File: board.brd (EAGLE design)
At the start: 25 x 23.8 mm, 31 parts, among them SW1 JST_SM02B-SRSS-TB, U2 FT232RQ, U3 ATTINY1607-MFR, U4 RV-8803, X2 JST_SM02B-SRSS-TB

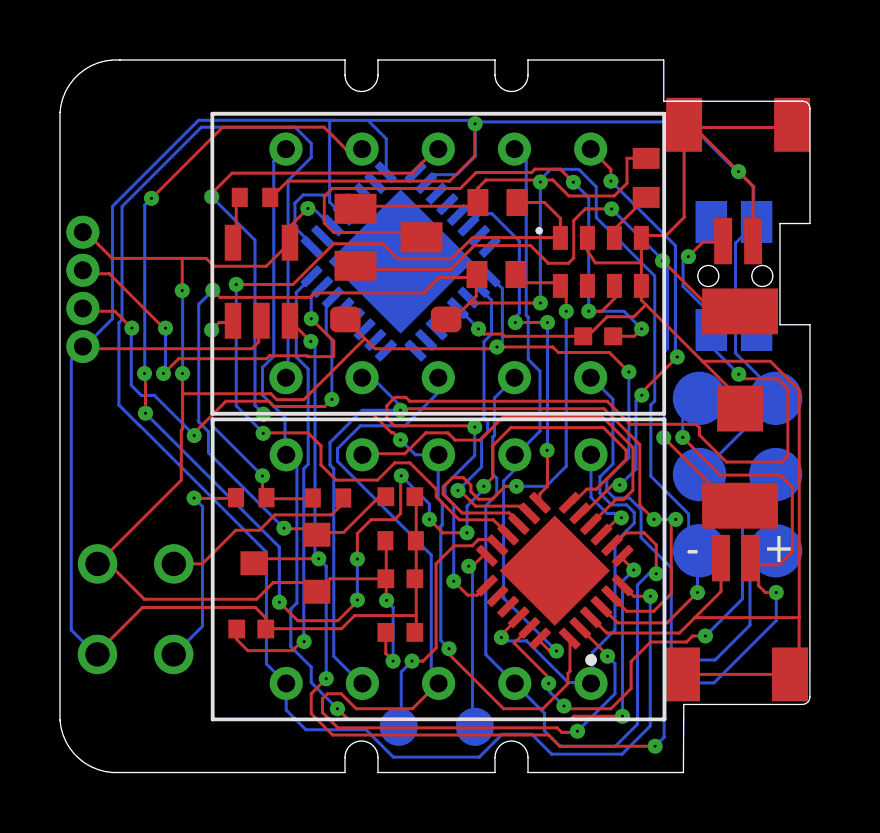
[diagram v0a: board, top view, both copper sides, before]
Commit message: 4 layer brd design for watch PCB added
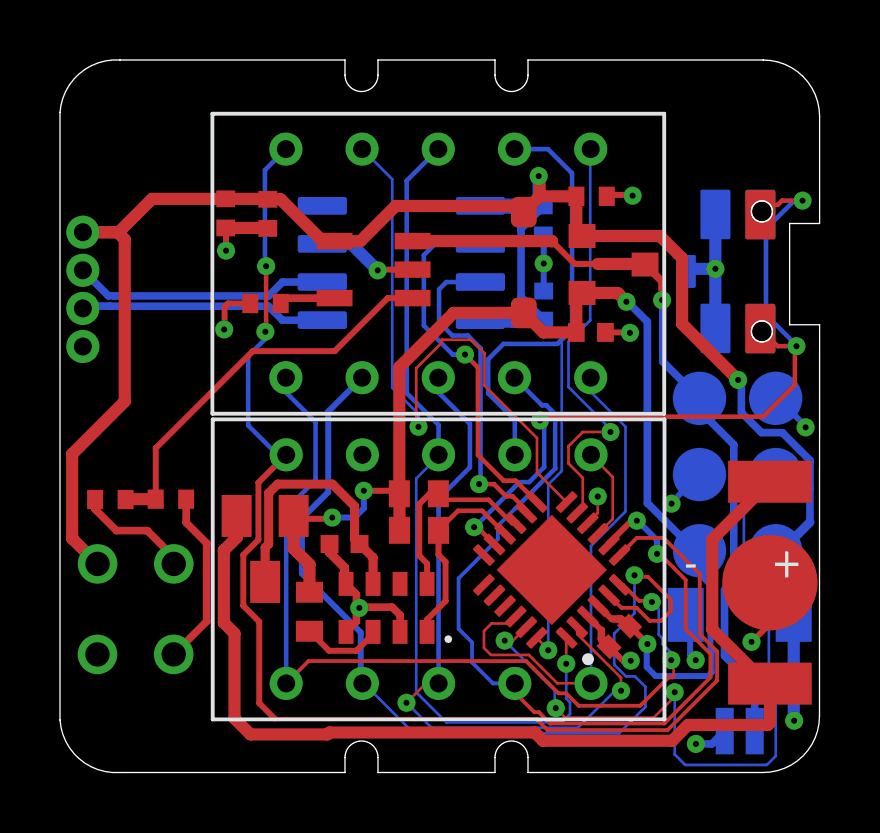
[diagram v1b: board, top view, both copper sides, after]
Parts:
- removed PC0, PC1: TESTPAD_TPSQB1,27, ARDUINO_3V_TTL_INTERFACE_2_PI:TESTPAD_B1,27
- removed SW1: JST_SM02B-SRSS-TB, MY_CLOCK_LIB_COMPONENTS:JST-SM02B-SRSS-TB
- removed U$9: EVQP7L01P, MY_CLOCK_LIB_COMPONENTS:EVQP7L01P
- removed U2: FT232RQ, FT232RQ:QFN50P500X500X90-33N
- added C3, C7: 100nF, MY_CAP_LIB:CAPC1005X60
- added U$4: PTS840ESDPMSMTRLF, MY_CLOCK_LIB_COMPONENTS:PTS840ESDPMSMTRLF
- added U$6: CH330N, MY_CLOCK_LIB_COMPONENTS:CH330N
- 1.55V-8MAH: value KEYSTONE-2294TR -> BK-414-TR; device MY_CLOCK_LIB_COMPONENTS:KEYSTONE-2994TR -> MY_CLOCK_LIB_COMPONENTS:BK-414-TR
- BOT, TOP: value 0.28"-2DIGIT-7SEGEMNT -> 0.28-2DIGIT-7SEGEMNT; device MY_CLOCK_LIB_COMPONENTS:2_DIGIT_0.28" -> MY_CLOCK_LIB_COMPONENTS:2_DIGIT_0.28
- moved R7 18.3 mm to (9.07, 6.11)
- moved C5 16.7 mm to (16.9, 19.2), flipped to the bottom, turned to 270 degrees
- moved C1 15.1 mm to (6.27, 19.4), turned to 270 degrees
- moved U$3 14.7 mm to (19.2, 17.7), turned to 270 degrees
- moved U4 13.6 mm to (11.6, 6.24), turned to 180 degrees
- moved R6 13.1 mm to (18.5, 20.0)
- moved C2 12.9 mm to (7.68, 19.4), turned to 270 degrees
- moved R4 11.2 mm to (12.7, 8.82)
- moved D2 11.2 mm to (7.59, 8.20), turned to 180 degrees
- moved C6 10.9 mm to (10.2, 8.37)
- moved C4 8.38 mm to (18.4, 15.4)
- moved R5 7.75 mm to (12.7, 10.0)
- moved R1 7.26 mm to (2.43, 9.85), turned to 0 degrees
- moved 1.55V-8MAH 5.89 mm to (24.4, 7.08)
- moved X2 5.77 mm to (23.4, 2.13), flipped to the bottom, turned to 0 degrees
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- renumbered BATTERY_CHARGED_GREEN to GREEN, BATT_CONNECTED_YELLOW to YELLOW
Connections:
- net N$2 renamed CHARGER_STAT
- net N$4 renamed LEDY_K
- net N$5 renamed CHARGER_PROG
- net N$6 renamed LEDG_A
- removed net EXP: U2.33
- removed net N$11: C5.1, U2.16
- removed net PC0: PC0.TP, U3.17
- removed net PC1: PC1.TP, U3.18
- removed net USBDM: U$5.P$2, U2.15
- removed net USBDP: U$5.P$3, U2.14
- new net USBD_N: U$5.USBD_N, U$6.D_N
- new net USBD_P: U$5.USBD_P, U$6.D_P
- net GND: now also 1.55V-8MAH.-, C3.2, C7.2, U$4.1, U$4.2, U$4.5, U$5.GND, U$6.GND; no longer 1.55V-8MAH.P$1, SW1.1, SW1.M1, SW1.M2, U$5.P$4, U$9.P$2, U2.17, U2.20, U2.24, U2.26, U2.4
- net RX: now also U$6.RXI; no longer U2.2
- net SW1: now also U$4.3, U$4.4, U$4.B3, U$4.B4, U3.17; no longer SW1.2, U$9.P$3, U3.19
- net TX: now also U$6.TXD; no longer U2.30
- net VBATT: now also 1.55V-8MAH.1+, 1.55V-8MAH.2+; no longer 1.55V-8MAH.P$2, 1.55V-8MAH.P$3
- net VCC: now also C7.1
- net V_USB: now also C3.1, C5.1, U$5.V_USB, U$6.V3, U$6.VCC; no longer U$5.P$1, U2.1, U2.19
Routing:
- net GND: track 151.7 -> 35.5 mm, vias 3 -> 15
- net COMM1: track 46.4 -> 21.0 mm, vias 10 -> 1
- net SEG_E: track 54.1 -> 29.4 mm, vias 1 -> 2
- net SCL: track 30.1 -> 6.55 mm, vias 2 -> 0
- net VCC: track 63.9 -> 41.4 mm, vias 5 -> 4
- net V_LIPO: track 46.7 -> 25.4 mm, vias 6 -> 1
- net N$11: track 15.5 -> 0.00 mm, vias 1 -> 0
- net USBDP: track 15.5 -> 0.00 mm, vias 3 -> 0
- net USBDM: track 13.8 -> 0.00 mm, vias 3 -> 0
- net V_USB: track 74.1 -> 60.6 mm, vias 7 -> 2
- net VDD1: track 22.2 -> 9.15 mm, vias 3 -> 0
- net SW1: track 35.5 -> 25.3 mm
- net SDA: track 16.1 -> 6.53 mm, vias 2 -> 0
- net VBATT: track 26.1 -> 35.2 mm, vias 3 -> 0
- net SEG_C: track 32.1 -> 23.1 mm
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- added copper zone on layer 15, net GND
- added copper zone on layer 2, net GND
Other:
- board size 25 x 23.8 mm -> 25.3 x 23.8 mm
- board text removed: "P7"
- board text removed: "P8"
